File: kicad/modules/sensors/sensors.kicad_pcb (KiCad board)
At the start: 2 copper layers, 84.6 x 64 mm, 61 parts, among them J1 Bus_PCI_Express_x1, J4 Conn_01x02, J6 USB_C_Receptacle_USB2.0_16P, U2 RP2040, U4 W25Q128JVP, U5 BMP388, U8 BNO055, U9 MCP25625T-E/ML, X1 ABM8-272-T3, Y1 ABS07-32.768KHZ-T, Y2 X322516MLB4SI

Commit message: sensors: generate final production files
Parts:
- moved J4 0.62 mm to (121.5, 117.6)
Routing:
- net GND: track 13.1 -> 19.1 mm
- net +7.4V: track 4.00 -> 0.00 mm
- net +5V: track 37.4 -> 41.2 mm
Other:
- board text added: "sensors 0.1.0"
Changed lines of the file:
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@@
 	(footprint "Connector_PinHeader_2.54mm:PinHeader_1x02_P2.54mm_Vertical"
 		(layer "F.Cu")
-		(at 121.46 118.25 90)
+		(at 121.46 117.625 90)
 		(descr "Through hole straight pin header, 1x02, 2.54mm pitch, single row")
 		(tags "Through hole pin header THT 1x02 2.54mm single row")
@@
 			(at 0 -1.16 90)
 			(layer "F.SilkS")
+			(hide yes)
 			(effects
 				(font
@@
 			(at 0 1.16 90)
 			(layer "F.Fab")
+			(hide yes)
 			(effects
 				(font
@@
 			(at 0 -1.16 90)
 			(layer "F.SilkS")
+			(hide yes)
 			(effects
 				(font
@@
 			(at 0 1.16 90)
 			(layer "F.Fab")
+			(hide yes)
 			(effects
 				(font
@@
 	)
 	(footprint "Connector_PCBEdge:BUS_PCIexpress_x1"
-		(locked yes)
 		(layer "B.Cu")
 		(at 136.913 64.138595)
@@
 		(layer "Edge.Cuts")
 	)
+	(gr_text "sensors 0.1.0"
+		(at 153 78 0)
+		(layer "F.SilkS")
+		(effects
+			(font
+				(size 1.5 1.5)
+				(thickness 0.3)
+				(bold yes)
+			)
+			(justify left bottom)
+		)
+	)
 	(segment
 		(start 145.75 93)
@@
 	)
 	(segment
-		(start 155.913 64.138595)
-		(end 153.913 64.138595)
-		(width 0.3)
-		(layer "F.Cu")
-		(net 2)
-	)
-	(segment
-		(start 155.913 64.138595)
-		(end 153.913 64.138595)
-		(width 0.3)
-		(layer "B.Cu")
-		(net 2)
-	)
-	(segment
 		(start 138.887999 90.438025)
 		(end 138.887999 93.387999)
@@
 	)
 	(segment
-		(start 141.0625 99.3125)
-		(end 143.6625 99.3125)
+		(start 138.75 97)
+		(end 141.0625 99.3125)
 		(width 0.15)
 		(layer "F.Cu")
@@
 	)
 	(segment
-		(start 138.75 97)
-		(end 141.0625 99.3125)
+		(start 141.0625 99.3125)
+		(end 143.6625 99.3125)
 		(width 0.15)
 		(layer "F.Cu")
@@
 	)
 	(segment
-		(start 136.25 97)
+		(start 134.5 97)
 		(end 138.75 97)
 		(width 0.15)
@@
 	)
 	(via
-		(at 136.25 97)
+		(at 134.5 97)
 		(size 0.4)
 		(drill 0.3)
@@
 	)
 	(segment
-		(start 132.25 95.25)
-		(end 134 97)
+		(start 134 97)
+		(end 132.25 95.25)
 		(width 0.15)
 		(layer "B.Cu")
@@
 	)
 	(segment
-		(start 134 97)
-		(end 136.25 97)
+		(start 134.5 97)
+		(end 134 97)
 		(width 0.15)
 		(layer "B.Cu")
@@
 	)
 	(segment
-		(start 132.805976 85.694024)
-		(end 132.25 86.25)
+		(start 132.25 86.25)
+		(end 132.805976 85.694024)
 		(width 0.15)
 		(layer "B.Cu")
@@
 	)
 	(segment
-		(start 132.25 86.25)
-		(end 132.25 95.25)
+		(start 132.25 95.25)
+		(end 132.25 86.25)
 		(width 0.15)
 		(layer "B.Cu")
@@
 	)
 	(segment
+		(start 142.913 64.138595)
+		(end 139.913 64.138595)
+		(width 0.5)
+		(layer "F.Cu")
+		(net 26)
+	)
+	(segment
 		(start 161.725 89.75)
 		(end 161.5875 89.8875)
@@
 		(start 138.75 100.975)
 		(end 137.79 100.975)
-		(width 0.15)
+		(width 0.2)
 		(layer "F.Cu")
 		(net 26)
@@
 	(segment
 		(start 142.913 64.138595)
-		(end 139.913 64.138595)
-		(width 0.3)
+		(end 136.913 64.138595)
+		(width 0.5)
 		(layer "B.Cu")
 		(net 26)
@@
 	)
 	(segment
-		(start 146.913 64.138595)
-		(end 144.913 64.138595)
-		(width 0.3)
-		(layer "F.Cu")
-		(net 56)
-	)
-	(segment
 		(start 136.5 101.265)
 		(end 136.235 101)
@@
 	)
 	(segment
+		(start 144.913 64.138595)
+		(end 146.913 64.138595)
+		(width 0.5)
+		(layer "F.Cu")
+		(net 56)
+	)
+	(segment
 		(start 134.79 101)
 		(end 134.5 100.71)
@@
 	)
 	(segment
-		(start 146.913 64.138595)
-		(end 144.913 64.138595)
-		(width 0.3)
-		(layer "B.Cu")
-		(net 56)
-	)
-	(segment
 		(start 146.5 82.5)
 		(end 146.5 89)
@@
 	)
 	(segment
+		(start 144.913 64.138595)
+		(end 146.913 64.138595)
+		(width 0.5)
+		(layer "B.Cu")
+		(net 56)
+	)
+	(segment
 		(start 155.925 92.65)
 		(end 154.825 93.75)
@@
 	)
 	(segment
+		(start 151.913 64.138595)
+		(end 151.912562 64.138157)
+		(width 0.6)
+		(layer "F.Cu")
+		(net 68)
+	)
+	(segment
 		(start 136.093999 88.294024)
 		(end 135 88.294024)
@@
 		(net 68)
 	)
+	(segment
+		(start 151.912562 64.138157)
+		(end 150.059553 64.138157)
+		(width 0.5)
+		(layer "F.Cu")
+		(net 68)
+	)
 	(via
 		(at 135 88.294024)
@@
 	)
 	(segment
+		(start 151.832276 64.140598)
+		(end 149.979267 64.140598)
+		(width 0.5)
+		(layer "B.Cu")
+		(net 68)
+	)
+	(segment
 		(start 150.913 69.587)
 		(end 150.913 64.138595)
@@
 	)
 	(segment
+		(start 124.5 117.125)
+		(end 124 117.625)
+		(width 0.15)
+		(layer "B.Cu")
+		(net 69)
+	)
+	(segment
 		(start 143.359816 92.5)
 		(end 142.75 92.5)
@@
 	(segment
 		(start 124.5 110.75)
-		(end 124.5 118)
+		(end 124.5 117.125)
 		(width 0.15)
 		(layer "B.Cu")
@@
 	)
 	(segment
-		(start 143.5 91.5)
-		(end 143 91.5)
+		(start 121.96 117.125)
+		(end 121.46 117.625)
 		(width 0.15)
 		(layer "B.Cu")
@@
 	(segment
 		(start 121.96 112.54)
-		(end 121.96 118)
+		(end 121.96 117.125)
+		(width 0.15)
+		(layer "B.Cu")
+		(net 70)
+	)
+	(segment
+		(start 143.5 91.5)
+		(end 143 91.5)
 		(width 0.15)
 		(layer "B.Cu")
@@
 	)
 	(segment
-		(start 138.0593 68.217296)
-		(end 138.913 67.363596)
+		(start 138.913 66.156149)
+		(end 138.913 64.138595)
 		(width 0.16)
 		(layer "F.Cu")
@@
 	)
 	(segment
-		(start 138.0593 84.671325)
-		(end 138.0593 68.217296)
+		(start 138.238 84.850025)
+		(end 138.0593 84.671325)
 		(width 0.16)
 		(layer "F.Cu")
@@
 	)
 	(segment
-		(start 138.238 84.850025)
-		(end 138.0593 84.671325)
+		(start 138.0593 84.671325)
+		(end 138.0593 67.009849)
 		(width 0.16)
 		(layer "F.Cu")
@@
 	)
 	(segment
-		(start 138.913 67.363596)
-		(end 138.913 64.138595)
+		(start 138.0593 67.009849)
+		(end 138.913 66.156149)
 		(width 0.16)
 		(layer "F.Cu")
@@
 	)
 	(segment
-		(start 137.7667 84.671324)
-		(end 137.7667 68.217296)
+		(start 137.7667 67)
+		(end 136.913 66.1463)
 		(width 0.16)
 		(layer "F.Cu")
@@
 	)
 	(segment
-		(start 137.587999 84.850025)
-		(end 137.7667 84.671324)
+		(start 136.913 66.1463)
+		(end 136.913 64.138595)
 		(width 0.16)
 		(layer "F.Cu")
@@
 	)
 	(segment
-		(start 136.913 67.363596)
-		(end 136.913 64.138595)
+		(start 137.7667 84.671324)
+		(end 137.7667 67)
 		(width 0.16)
 		(layer "F.Cu")
@@
 	)
 	(segment
-		(start 137.7667 68.217296)
-		(end 136.913 67.363596)
+		(start 137.587999 84.850025)
+		(end 137.7667 84.671324)
 		(width 0.16)
 		(layer "F.Cu")

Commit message: revise production files
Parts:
- removed ? (x9): , 

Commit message: revise production files again
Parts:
- added ?: , , F.Cu at (145.8, 99.6)
- added ?: , , F.Cu at (148.4, 97.0)
- added ?: , , F.Cu at (145.8, 97.0)
- added ?: , , F.Cu at (147.1, 98.3)
- added ?: , , F.Cu at (145.8, 98.3)
- added ?: , , F.Cu at (148.4, 98.3)
- added ?: , , F.Cu at (147.1, 99.6)
- added ?: , , F.Cu at (147.1, 97.0)
- added ?: , , F.Cu at (148.4, 99.6)

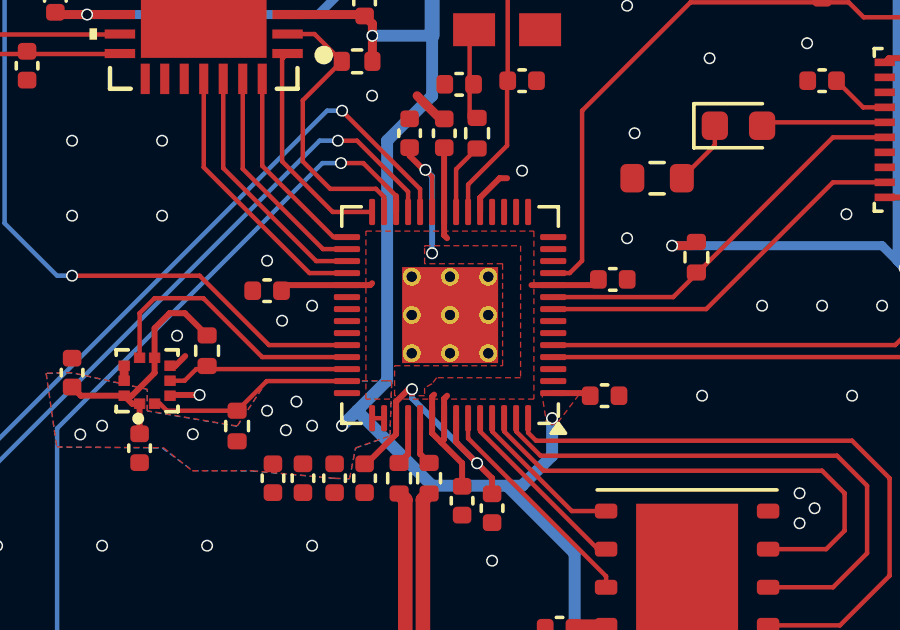
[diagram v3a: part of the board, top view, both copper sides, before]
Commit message: sensors: update vias under rp2040
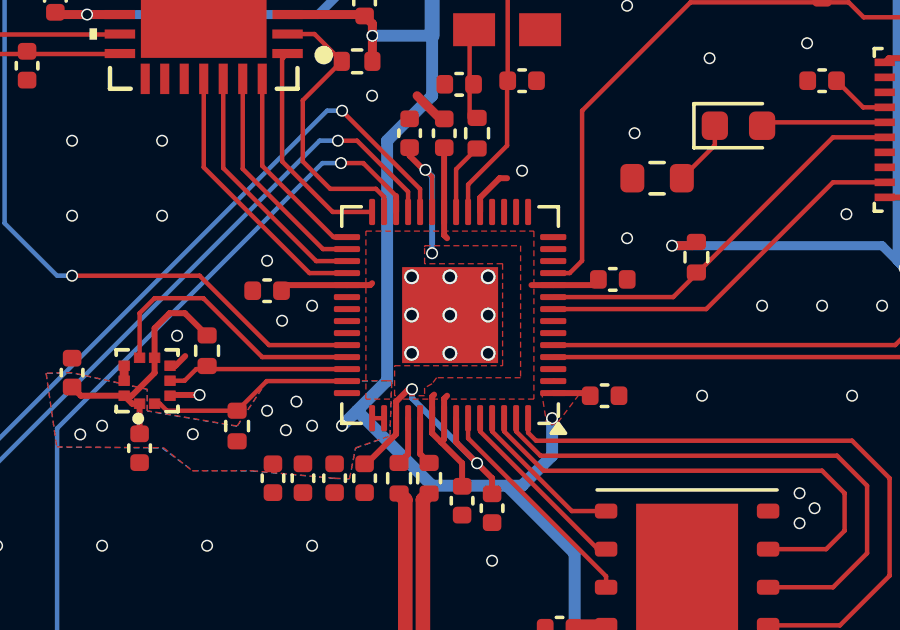
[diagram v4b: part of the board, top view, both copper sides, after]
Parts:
- removed ? (x9): , 
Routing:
- net GND: vias 193 -> 202
